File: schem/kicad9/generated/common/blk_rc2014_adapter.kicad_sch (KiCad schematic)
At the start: 0 parts

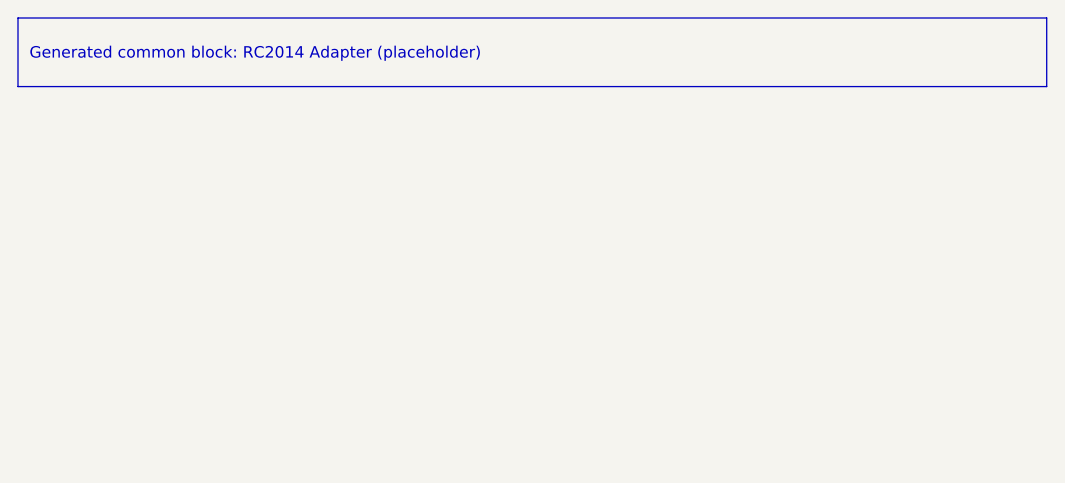
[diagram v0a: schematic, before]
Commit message: kicad: add carbon block symbol library + docs + regen scripts
Detailed description:
- What was implemented: added schem/kicad9/libs/carbon_blocks.kicad_sym placeholder symbols, schem/kicad9/docs/USAGE.md, and scripts/gen_kicad.ps1 plus scripts/gen_kicad.sh; generator now embeds and uses carbon_blocks symbols in generated common block sheets and adds a JTAG/UART common block to system tops.
- Why it exists: keeps the generated hierarchy self-contained and makes regeneration repeatable while reserving a clear path to later map blocks to real parts.
- Architectural assumptions: generator overwrites only schem/kicad9/generated/; carbon_blocks symbols are placeholders (no pin-level mapping in v1); common blocks are represented as simple symbols inside common subsheets.
- How to run it: scripts/gen_kicad.ps1 or scripts/gen_kicad.sh (or python tools/kicadgen/src/kicadgen.py).
- What is NOT implemented yet: automatic mapping to specific 74ACT parts and real footprints, detailed per-net wiring between blocks, and deeper parsing of hdl/spec YAML beyond the mapping specs.
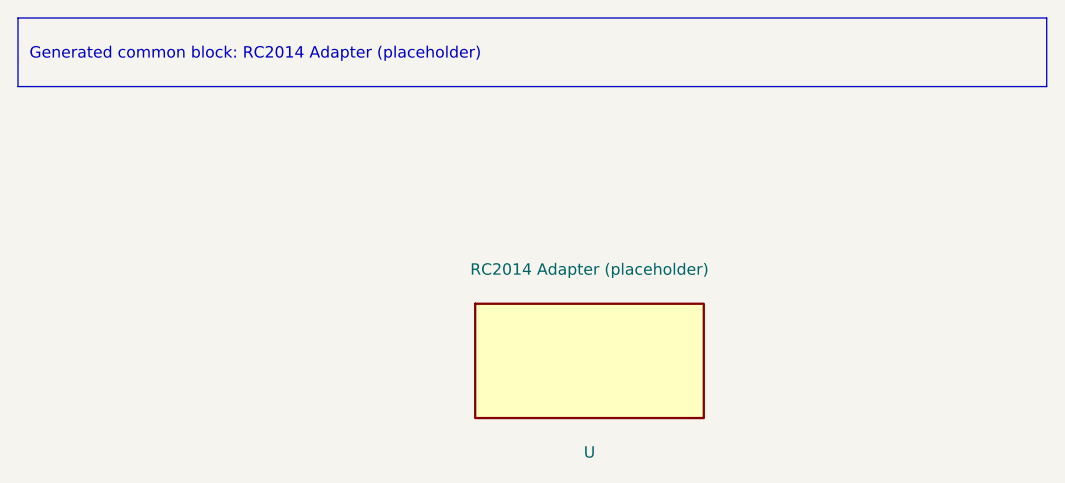
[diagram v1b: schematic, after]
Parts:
- added U: RC2014 Adapter (placeholder), symbol carbon_blocks:CARBON_BLOCK_RC2014_ADAPTER
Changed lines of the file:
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@@
+		)
+	)
+	(symbol
+		(lib_id "carbon_blocks:CARBON_BLOCK_RC2014_ADAPTER")
+		(at
+			76.2
+			50.8
+			0
+		)
+		(unit 1)
+		(exclude_from_sim no)
+		(in_bom yes)
+		(on_board yes)
+		(dnp no)
+		(property
+			"Reference"
+			"U"
+			(at
+				76.2
+				60.96
+				0
+			)
+			(effects
+				(font
+					(size 1.27 1.27)
+				)
+			)
+		)
+		(property
+			"Value"
+			"RC2014 Adapter (placeholder)"
+			(at
+				76.2
+				40.64
+				0
+			)
+			(effects
+				(font
+					(size 1.27 1.27)
+				)
+			)
+		)
+		(property
+			"Footprint"
+			""
+			(at
+				76.2
+				50.8
+				0
+			)
+			(effects
+				(font
+					(size 1.27 1.27)
+				)
+				(hide yes)
+			)
+		)
+		(property
+			"Datasheet"
+			""
+			(at
+				76.2
+				50.8
+				0
+			)
+			(effects
+				(font
+					(size 1.27 1.27)
+				)
+				(hide yes)
+			)
+		)
+		(property
+			"Description"
+			""
+			(at
+				76.2
+				50.8
+				0
+			)
+			(effects
+				(font
+					(size 1.27 1.27)
+				)
+				(hide yes)
+			)
+		)
+		(instances
+			(project
+				"carbon_common"
+				(path
+					"/4042ec75-81d2-5b64-add8-dc01e9db4e94"
+					(reference "U")
+					(unit 1)
+				)
+			)
 		)
 	)
